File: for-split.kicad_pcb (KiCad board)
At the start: 2 copper layers, 114.3 x 95.3 mm, 84 parts, among them J1 TRRS, J2 TRRS, U1 ProMicro

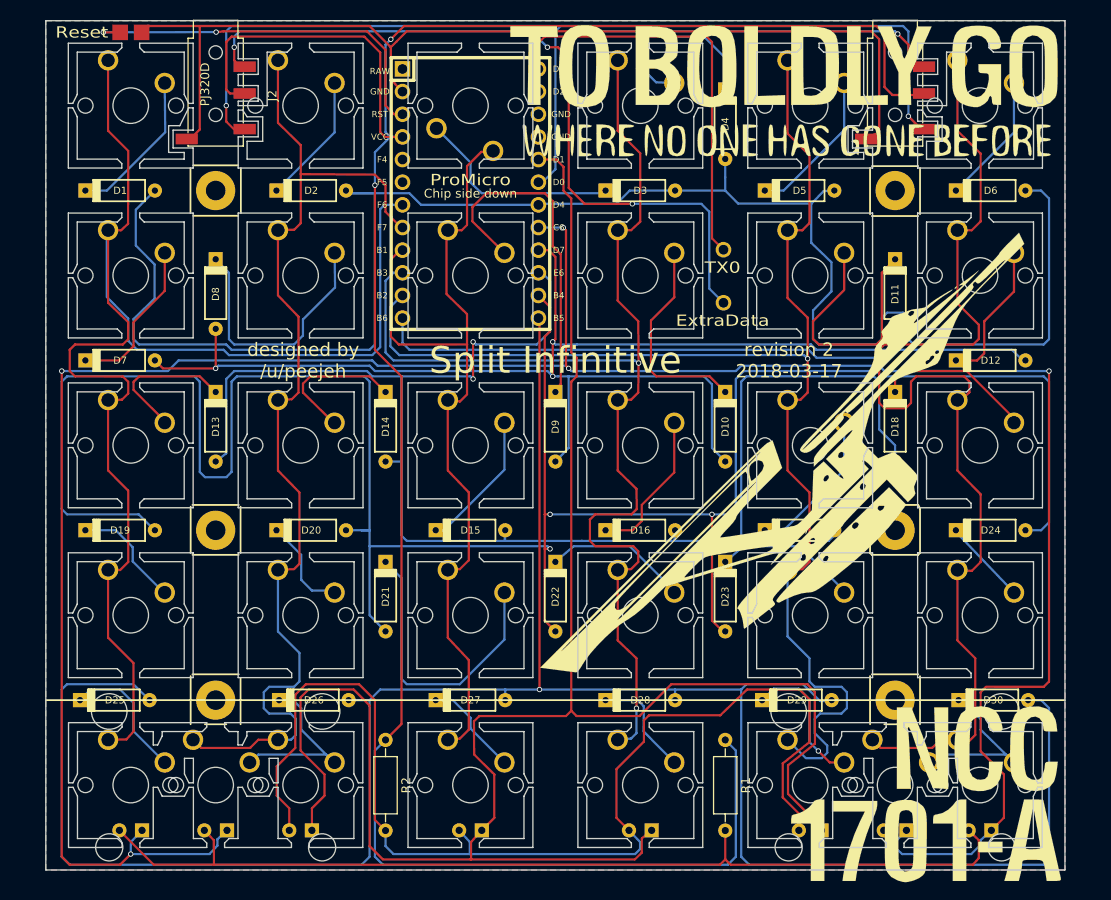
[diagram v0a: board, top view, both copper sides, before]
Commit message: Fix incorrect LED routing
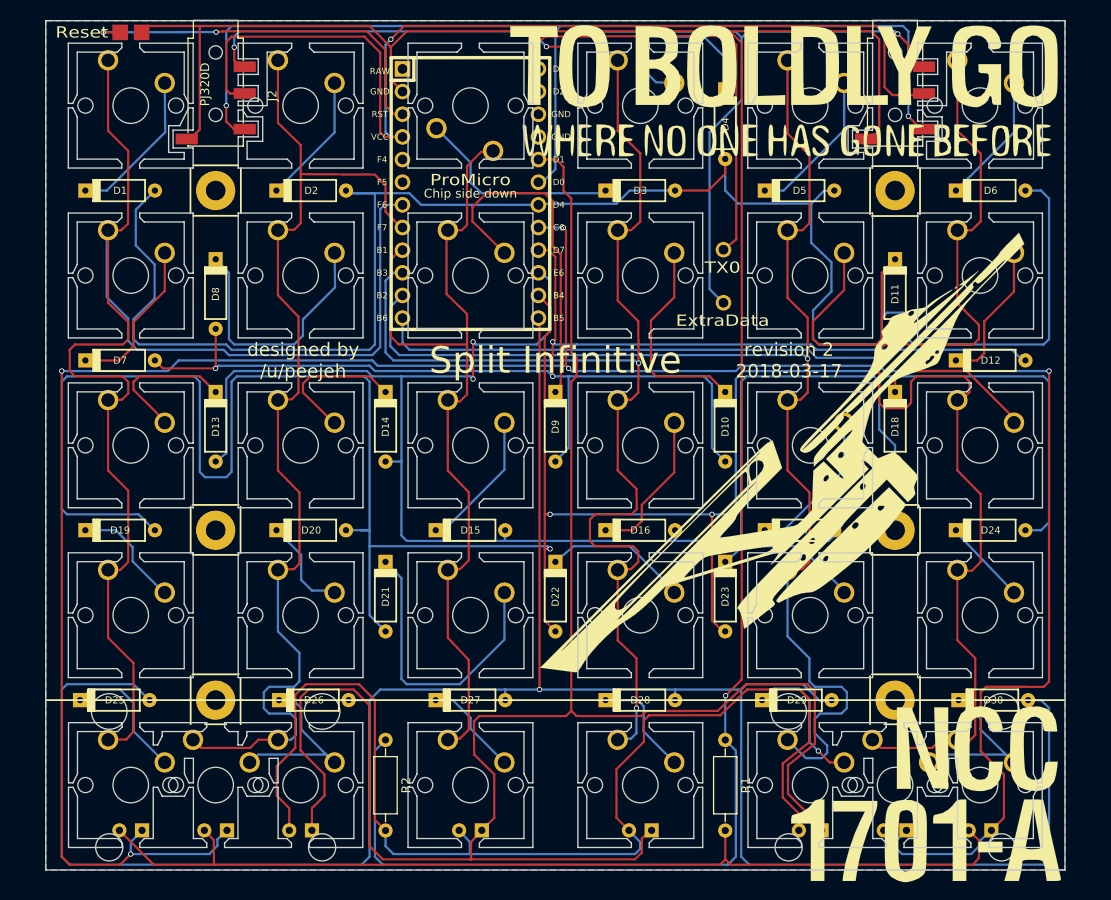
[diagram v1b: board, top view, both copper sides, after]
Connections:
- R1 pad 1: VCC -> GND
- R2 pad 1: VCC -> GND
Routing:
- net GND: track 116.8 -> 265.9 mm, vias 0 -> 1
- net VCC: track 257.4 -> 118.6 mm, vias 2 -> 1
- net Net-(EXTRADATA1-Pad1): track 130.3 -> 118.1 mm, vias 5 -> 4
- net Net-(TX0-Pad1): track 46.8 -> 49.5 mm
- net /Row0: track 197.2 -> 199.6 mm

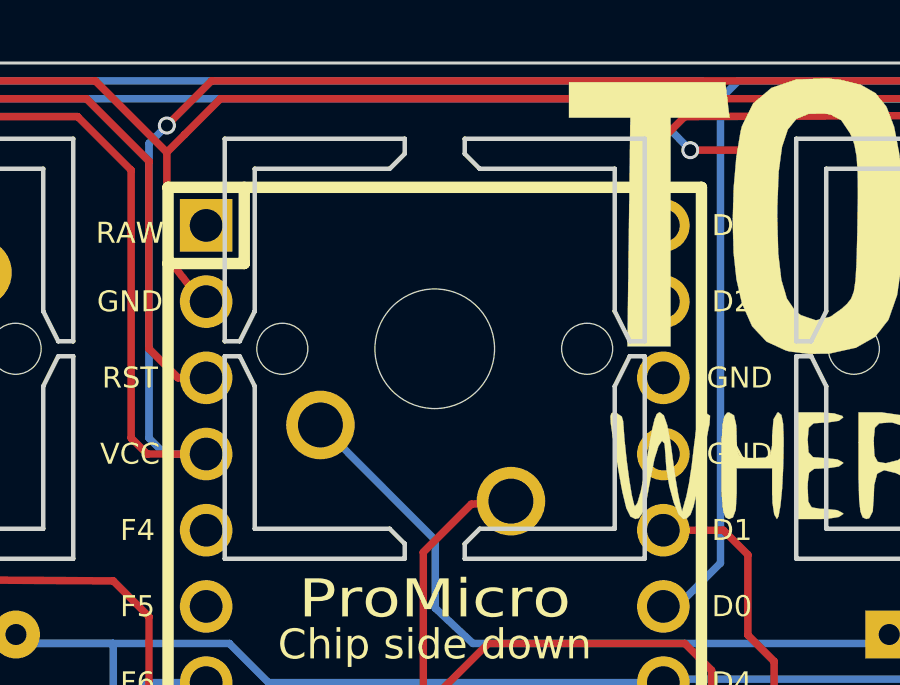
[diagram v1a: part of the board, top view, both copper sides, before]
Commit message: Add north/south facing option for switch under ProMicro
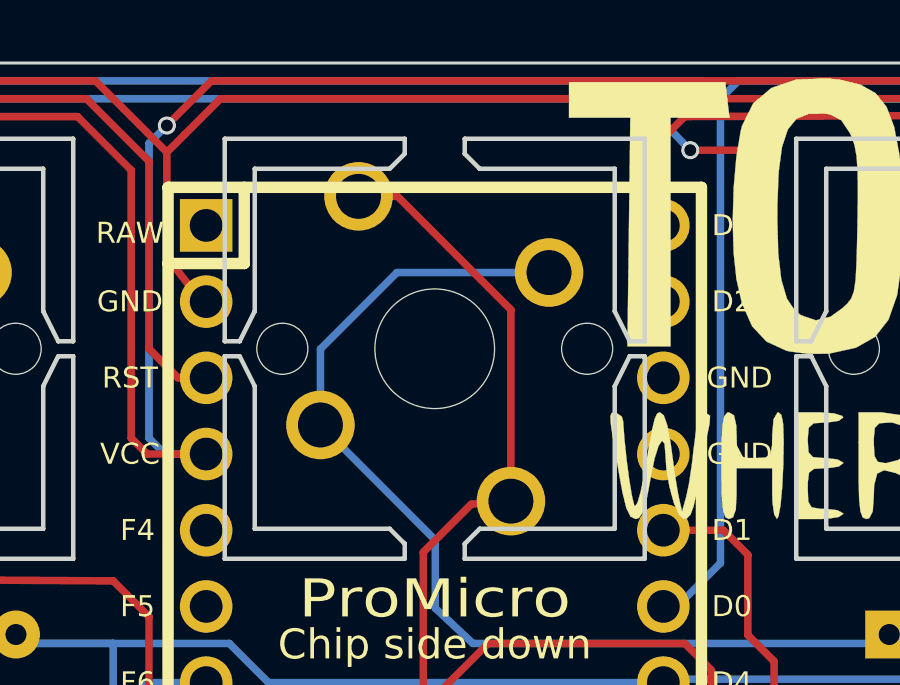
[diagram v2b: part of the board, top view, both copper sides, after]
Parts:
- MX0:2: footprint idle-hands:MX_CUTOUT -> idle-hands:MX_CUTOUT_NTHSTH
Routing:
- net /Col2: track 97.1 -> 110.1 mm
- net Net-(D3-Pad1): track 23.4 -> 34.6 mm

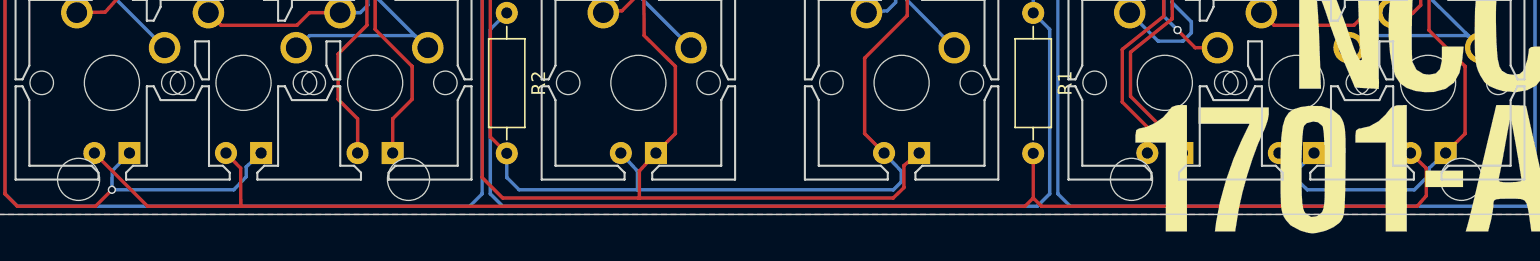
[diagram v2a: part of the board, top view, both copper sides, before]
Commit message: Flip LED footprints to correct orientation
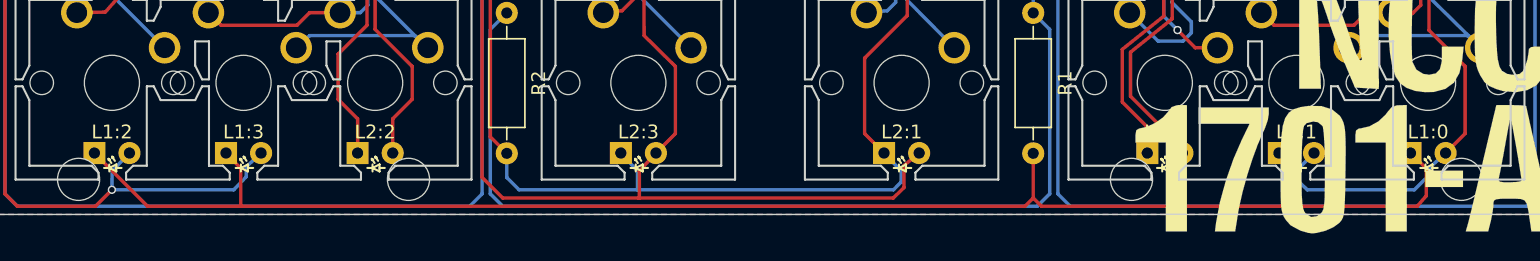
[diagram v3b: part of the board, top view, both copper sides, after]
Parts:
- L1:0, L1:1, L1:2, L1:3, L2:0, L2:1, L2:2, L2:3: moved to F.Cu
- turned L1:0 to 0 degrees
- turned L1:1 to 0 degrees
- turned L1:2 to 0 degrees
- turned L1:3 to 0 degrees
- turned L2:0 to 0 degrees
- turned L2:1 to 0 degrees
- turned L2:2 to 0 degrees
- turned L2:3 to 0 degrees
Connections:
- L1:0 pad 1: /LED1 -> Net-(L1:0-Pad1)
- L1:0 pad 2: Net-(L1:0-Pad2) -> /LED1
- L1:1 pad 1: /LED1 -> Net-(L1:0-Pad1)
- L1:1 pad 2: Net-(L1:0-Pad2) -> /LED1
- L1:2 pad 1: /LED1 -> Net-(L1:0-Pad1)
- L1:2 pad 2: Net-(L1:0-Pad2) -> /LED1
- L1:3 pad 1: /LED1 -> Net-(L1:0-Pad1)
- L1:3 pad 2: Net-(L1:0-Pad2) -> /LED1
- L2:0 pad 1: /LED2 -> Net-(L2:0-Pad1)
- L2:0 pad 2: Net-(L2:0-Pad2) -> /LED2
- L2:1 pad 1: /LED2 -> Net-(L2:0-Pad1)
- L2:1 pad 2: Net-(L2:0-Pad2) -> /LED2
- L2:2 pad 1: /LED2 -> Net-(L2:0-Pad1)
- L2:2 pad 2: Net-(L2:0-Pad2) -> /LED2
- L2:3 pad 1: /LED2 -> Net-(L2:0-Pad1)
- L2:3 pad 2: Net-(L2:0-Pad2) -> /LED2
- R1 pad 2: Net-(L1:0-Pad2) -> Net-(L1:0-Pad1)
- R2 pad 2: Net-(L2:0-Pad2) -> Net-(L2:0-Pad1)
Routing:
- net Net-(L2:0-Pad2): track 130.1 -> 0.00 mm
- net Net-(L2:0-Pad1): track 0.00 -> 130.1 mm
- net Net-(L1:0-Pad2): track 114.5 -> 0.00 mm
- net Net-(L1:0-Pad1): track 0.00 -> 114.5 mm

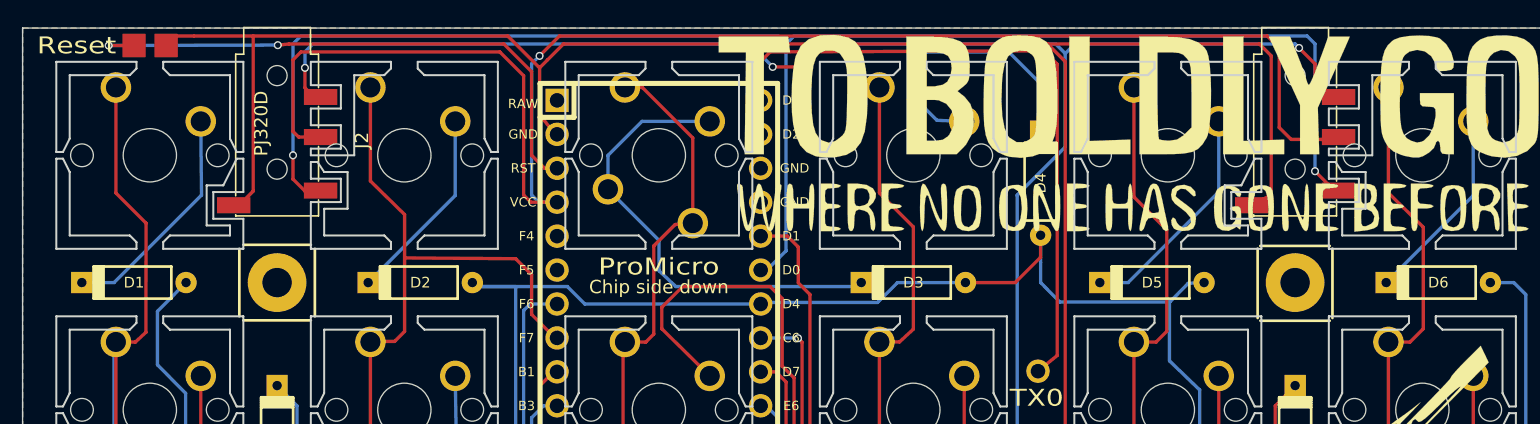
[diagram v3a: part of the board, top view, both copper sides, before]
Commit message: Add custom PJ320D footprint with larger pads
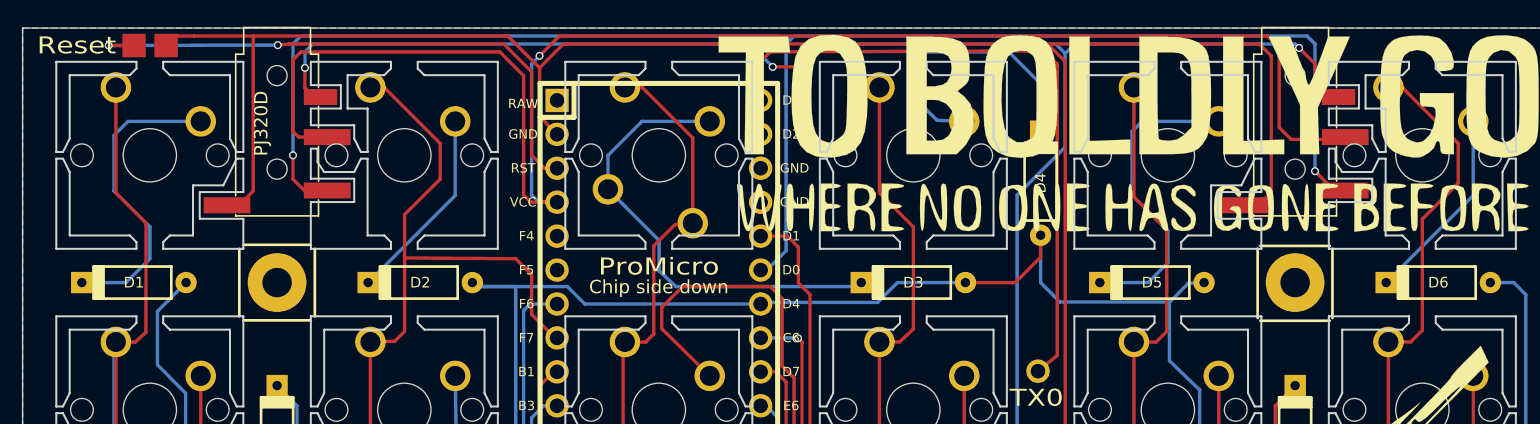
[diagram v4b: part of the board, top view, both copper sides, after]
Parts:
- J1, J2: footprint Connectors:PJ320D_3.5mm_Jack -> idle-hands:PJ320D_BigFoot
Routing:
- net Net-(D5-Pad1): track 17.0 -> 23.4 mm
- net Net-(D1-Pad1): track 17.2 -> 23.1 mm
- net /Col1: track 119.8 -> 122.5 mm
- net /Col5: track 180.5 -> 183.2 mm

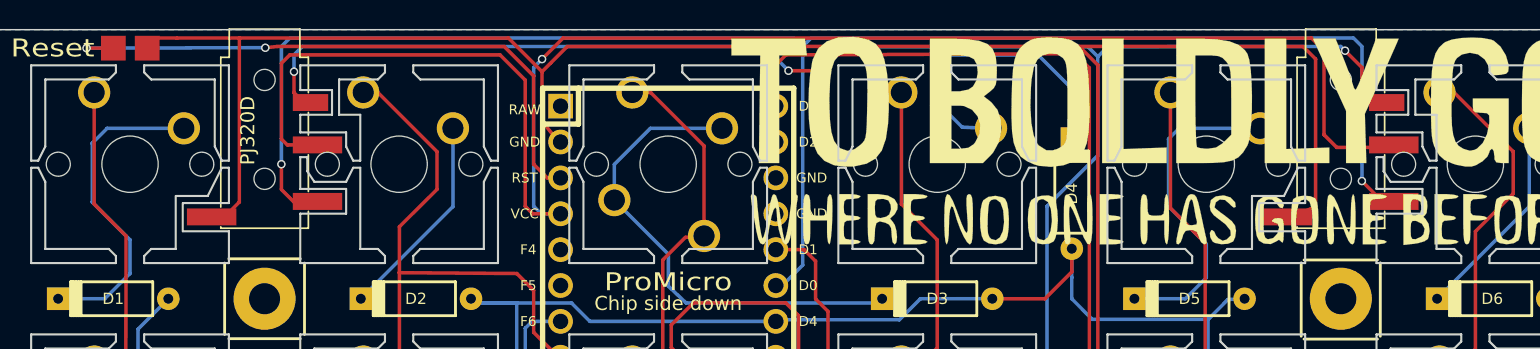
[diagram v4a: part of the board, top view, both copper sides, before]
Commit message: Switch to through hole PJ320A socket
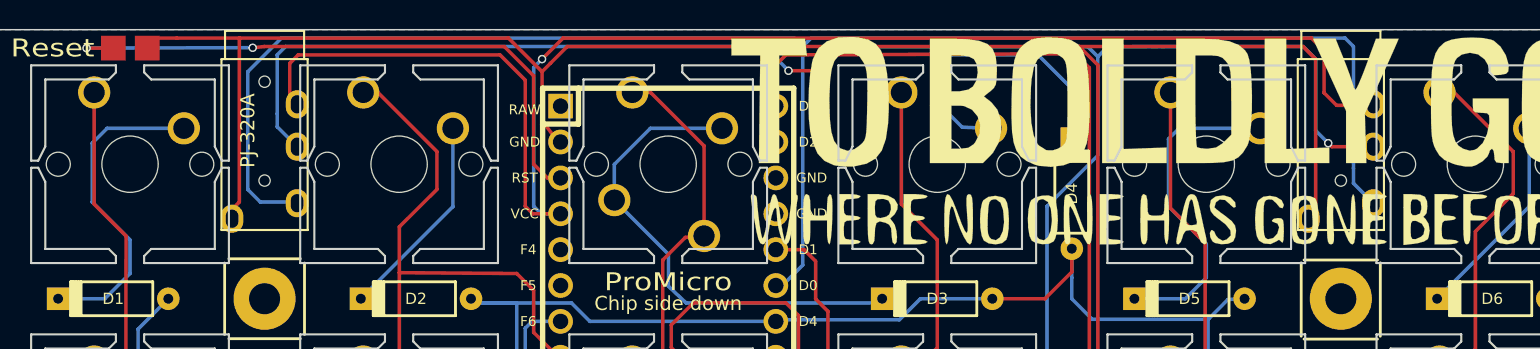
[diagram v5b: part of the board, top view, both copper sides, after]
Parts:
- J1: footprint idle-hands:PJ320D_BigFoot -> Keebio-Parts:TRRS-PJ-320A
- J2: footprint idle-hands:PJ320D_BigFoot -> idle-hands:PJ-320A
- MX0:0, MX0:4: footprint idle-hands:MX_CUTOUT_PAD1 -> idle-hands:MX_CUTOUT
- MX0:1, MX0:5: footprint idle-hands:MX_CUTOUT_PAD3 -> idle-hands:MX_CUTOUT
- moved J1 6.25 mm to (202.4, 66.4), turned to 0 degrees
- moved J2 6.25 mm to (126.2, 66.4), turned to 0 degrees
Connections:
- J1 pad 1: Net-(J1-Pad1) -> GND
- J1 pad 2: VCC -> Net-(J1-Pad2)
- J1 pad 4: GND -> VCC
- J2 pad 1: Net-(J1-Pad1) -> GND
- J2 pad 2: VCC -> Net-(J1-Pad2)
- J2 pad 4: GND -> VCC
- U1 pad 18: Net-(J1-Pad1) -> Net-(J1-Pad2)
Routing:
- net Net-(J1-Pad2): track 0.00 -> 121.8 mm
- net Net-(J1-Pad1): track 119.6 -> 0.00 mm, vias 2 -> 0
- net VCC: track 118.6 -> 109.2 mm
- net Net-(EXTRADATA1-Pad1): track 118.1 -> 124.8 mm, vias 4 -> 3
- net GND: track 265.9 -> 264.1 mm
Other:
- board text added: "PJ-320A"
- board text removed: "PJ320D"
